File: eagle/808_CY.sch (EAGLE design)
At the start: 115 parts, among them IC1 TL071P, IC2 TL071P, IC3 TL071P, IC4 TL072P, Q1 2N3904, Q2 2N3904, Q3 2N3904, Q4 2N3904, Q5 2N3904, Q6 2N3904, Q7 2N3904, Q8 2N3906

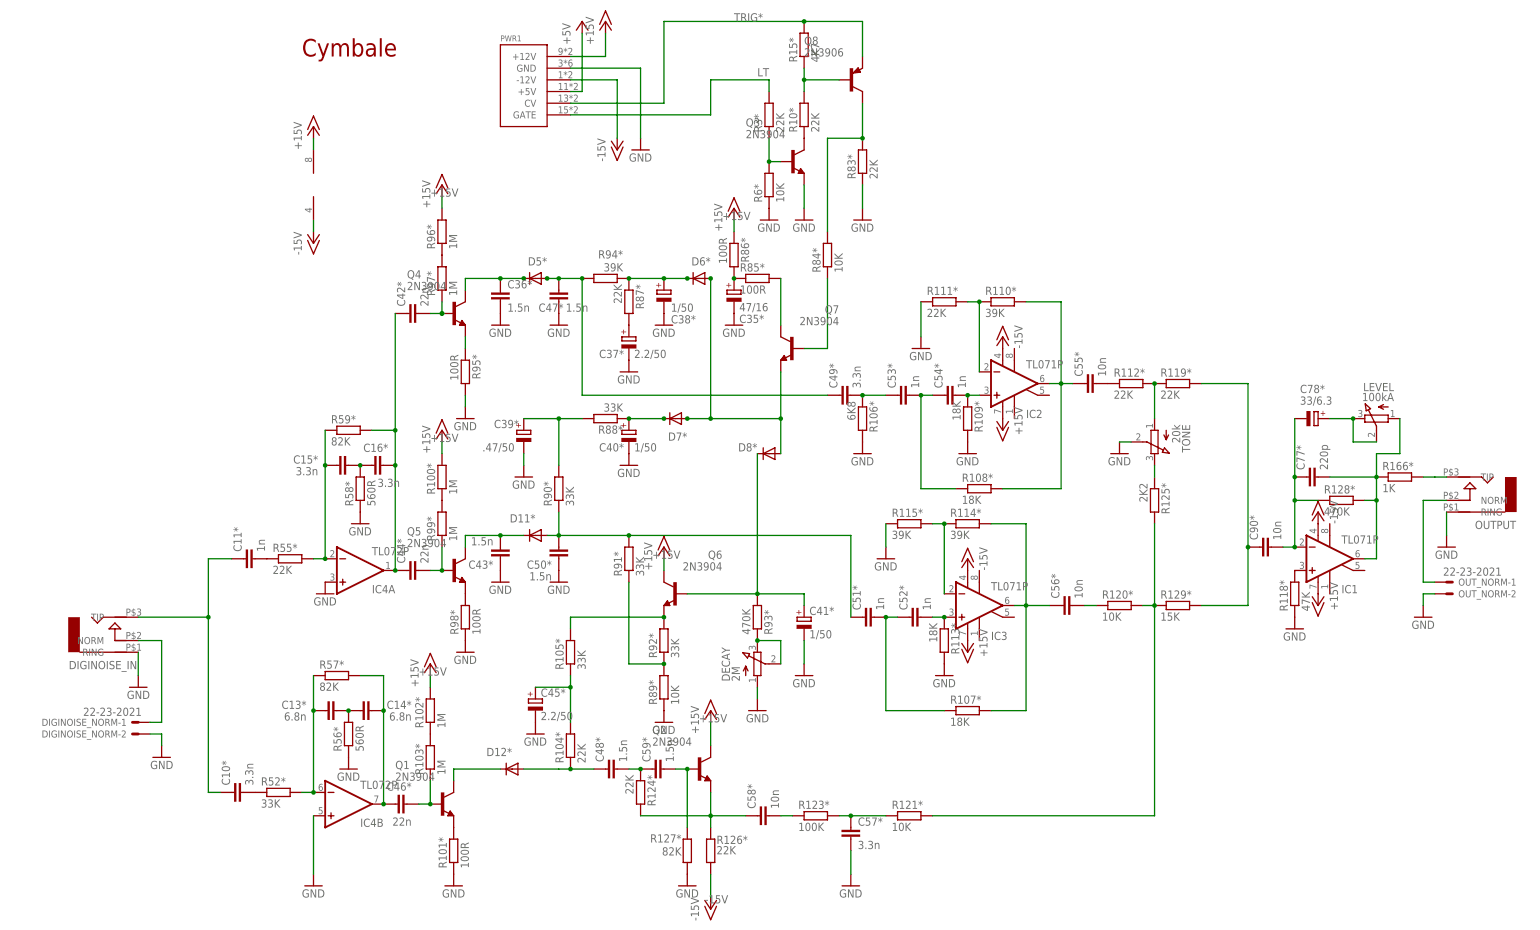
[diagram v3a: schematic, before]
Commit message: consolidated double 1m resistors
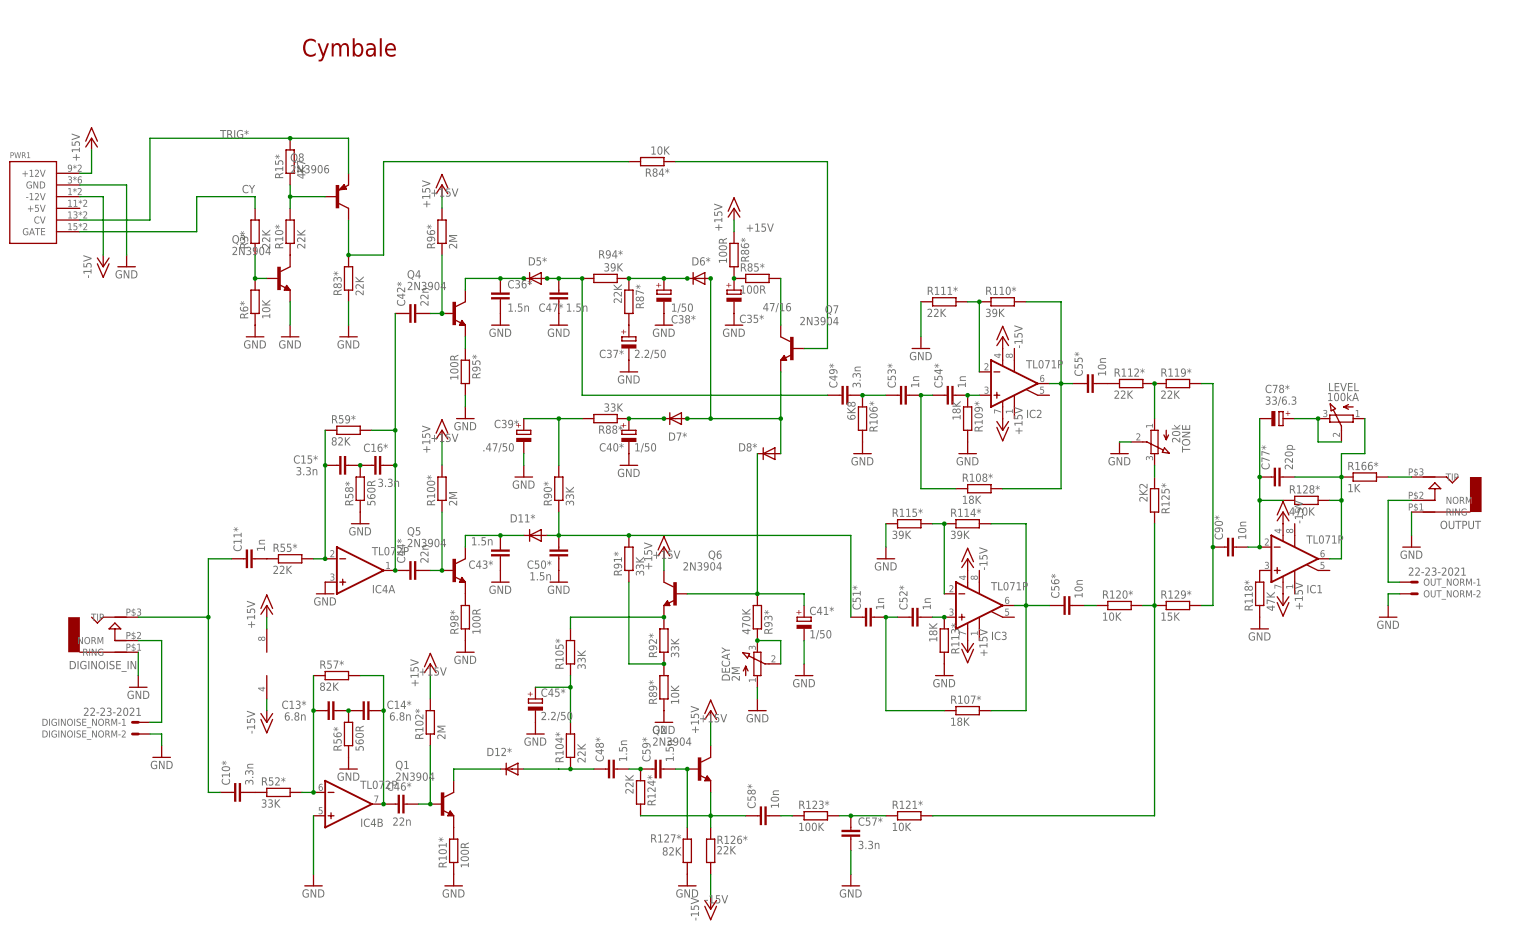
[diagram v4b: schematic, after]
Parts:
- removed R103*: 1M, TR808clone:R-EU_0207/2V
- removed R97*, R99*: 1M, TR808clone:R-EU_0207/5V
- R100*, R102*, R96*: value 1M -> 2M
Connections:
- net LT renamed CY
- removed net +5V: PWR1.+5V
- removed net CY_OUT: R166*.2
- removed net LT_LC_OUT: OUTPUT.TIP
- removed net N$176: R102*.1, R103*.2
- removed net N$180: R100*.1, R99*.2
- removed net N$181: R96*.1, R97*.2
- new net N$7: OUTPUT.TIP, R166*.2
- net N$498: now also R100*.1; no longer R99*.1
- net N$505: now also R102*.1; no longer R103*.1
- net N$524: now also R96*.1; no longer R97*.1
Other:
- moved on the sheet: C77*, C78*, C90*, IC1, LEVEL, OUTPUT, OUT_NORM-1, OUT_NORM-2, PWR1, Q3, Q8, R10*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

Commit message: third of the parts on
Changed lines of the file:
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@@
 <sheet>
 <plain>
-<text x="-33.02" y="149.86" size="3.81" layer="94">Cymbale</text>
+<text x="137.16" y="121.92" size="3.81" layer="94">Cymbale</text>
 </plain>
 <instances>

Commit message: 90 pct routed
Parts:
- R100*, R101*, R110*: device TR808clone:R-EU_0207/2V -> TR808clone:R-EU_0207/7
- R115*: device TR808clone:R-EU_0207/5V -> TR808clone:R-EU_0207/7
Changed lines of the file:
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@@
 <grid distance="0.1" unitdist="inch" unit="inch" style="lines" multiple="1" display="no" altdistance="0.01" altunitdist="inch" altunit="inch"/>
 <layers>
-<layer number="1" name="Top" color="1" fill="1" visible="no" active="no"/>
-<layer number="16" name="Bottom" color="4" fill="1" visible="no" active="no"/>
-<layer number="17" name="Pads" color="2" fill="1" visible="no" active="no"/>
-<layer number="18" name="Vias" color="2" fill="1" visible="no" active="no"/>
-<layer number="19" name="Unrouted" color="6" fill="1" visible="no" active="no"/>
-<layer number="20" name="Dimension" color="15" fill="1" visible="no" active="no"/>
-<layer number="21" name="tPlace" color="7" fill="1" visible="no" active="no"/>
-<layer number="22" name="bPlace" color="7" fill="1" visible="no" active="no"/>
-<layer number="23" name="tOrigins" color="15" fill="1" visible="no" active="no"/>
-<layer number="24" name="bOrigins" color="15" fill="1" visible="no" active="no"/>
-<layer number="25" name="tNames" color="7" fill="1" visible="no" active="no"/>
-<layer number="26" name="bNames" color="7" fill="1" visible="no" active="no"/>
-<layer number="27" name="tValues" color="7" fill="1" visible="no" active="no"/>
-<layer number="28" name="bValues" color="7" fill="1" visible="no" active="no"/>
-<layer number="29" name="tStop" color="7" fill="6" visible="no" active="no"/>
-<layer number="30" name="bStop" color="7" fill="3" visible="no" active="no"/>
-<layer number="31" name="tCream" color="7" fill="5" visible="no" active="no"/>
-<layer number="32" name="bCream" color="7" fill="4" visible="no" active="no"/>
+<layer number="1" name="Top" color="4" fill="1" visible="yes" active="no"/>
+<layer number="16" name="Bottom" color="1" fill="1" visible="yes" active="no"/>
+<layer number="17" name="Pads" color="2" fill="1" visible="yes" active="no"/>
+<layer number="18" name="Vias" color="2" fill="1" visible="yes" active="no"/>
+<layer number="19" name="Unrouted" color="6" fill="1" visible="yes" active="no"/>
+<layer number="20" name="Dimension" color="15" fill="1" visible="yes" active="no"/>
+<layer number="21" name="tPlace" color="7" fill="1" visible="yes" active="no"/>
+<layer number="22" name="bPlace" color="7" fill="1" visible="yes" active="no"/>
+<layer number="23" name="tOrigins" color="15" fill="1" visible="yes" active="no"/>
+<layer number="24" name="bOrigins" color="15" fill="1" visible="yes" active="no"/>
+<layer number="25" name="tNames" color="7" fill="1" visible="yes" active="no"/>
+<layer number="26" name="bNames" color="7" fill="1" visible="yes" active="no"/>
+<layer number="27" name="tValues" color="7" fill="1" visible="yes" active="no"/>
+<layer number="28" name="bValues" color="7" fill="1" visible="yes" active="no"/>
+<layer number="29" name="tStop" color="7" fill="3" visible="no" active="no"/>
+<layer number="30" name="bStop" color="7" fill="6" visible="no" active="no"/>
+<layer number="31" name="tCream" color="7" fill="4" visible="no" active="no"/>
+<layer number="32" name="bCream" color="7" fill="5" visible="no" active="no"/>
 <layer number="33" name="tFinish" color="6" fill="3" visible="no" active="no"/>
 <layer number="34" name="bFinish" color="6" fill="6" visible="no" active="no"/>
 <layer number="35" name="tGlue" color="7" fill="4" visible="no" active="no"/>
 <layer number="36" name="bGlue" color="7" fill="5" visible="no" active="no"/>
-<layer number="37" name="tTest" color="7" fill="1" visible="no" active="no"/>
-<layer number="38" name="bTest" color="7" fill="1" visible="no" active="no"/>
+<layer number="37" name="tTest" color="7" fill="1" visible="yes" active="no"/>
+<layer number="38" name="bTest" color="7" fill="1" visible="yes" active="no"/>
 <layer number="39" name="tKeepout" color="4" fill="11" visible="no" active="no"/>
 <layer number="40" name="bKeepout" color="1" fill="11" visible="no" active="no"/>
@@
 <layer number="44" name="Drills" color="7" fill="1" visible="no" active="no"/>
 <layer number="45" name="Holes" color="7" fill="1" visible="no" active="no"/>
-<layer number="46" name="Milling" color="3" fill="1" visible="no" active="no"/>
-<layer number="47" name="Measures" color="7" fill="1" visible="no" active="no"/>
-<layer number="48" name="Document" color="7" fill="1" visible="no" active="no"/>
-<layer number="49" name="Reference" color="7" fill="1" visible="no" active="no"/>
-<layer number="50" name="dxf" color="7" fill="1" visible="no" active="no"/>
-<layer number="51" name="tDocu" color="7" fill="1" visible="no" active="no"/>
-<layer number="52" name="bDocu" color="7" fill="1" visible="no" active="no"/>
-<layer number="53" name="tGND_GNDA" color="7" fill="9" visible="no" active="no"/>
-<layer number="54" name="bGND_GNDA" color="1" fill="9" visible="no" active="no"/>
-<layer number="56" name="wert" color="7" fill="1" visible="no" active="no"/>
-<layer number="57" name="tCAD" color="7" fill="1" visible="no" active="no"/>
-<layer number="59" name="tCarbon" color="7" fill="1" visible="no" active="no"/>
-<layer number="60" name="bCarbon" color="7" fill="1" visible="no" active="no"/>
+<layer number="46" name="Milling" color="3" fill="1" visible="yes" active="no"/>
+<layer number="47" name="Measures" color="7" fill="1" visible="yes" active="no"/>
+<layer number="48" name="Document" color="7" fill="1" visible="yes" active="no"/>
+<layer number="49" name="Reference" color="7" fill="1" visible="yes" active="no"/>
+<layer number="50" name="dxf" color="7" fill="1" visible="yes" active="no"/>
+<layer number="51" name="tDocu" color="7" fill="1" visible="yes" active="no"/>
+<layer number="52" name="bDocu" color="7" fill="1" visible="yes" active="no"/>
+<layer number="53" name="tGND_GNDA" color="7" fill="9" visible="yes" active="no"/>
+<layer number="54" name="bGND_GNDA" color="1" fill="9" visible="yes" active="no"/>
+<layer number="56" name="wert" color="7" fill="1" visible="yes" active="no"/>
+<layer number="57" name="tCAD" color="7" fill="1" visible="yes" active="no"/>
+<layer number="59" name="tCarbon" color="7" fill="1" visible="yes" active="no"/>
+<layer number="60" name="bCarbon" color="7" fill="1" visible="yes" active="no"/>
 <layer number="90" name="Modules" color="5" fill="1" visible="yes" active="yes"/>
 <layer number="91" name="Nets" color="2" fill="1" visible="yes" active="yes"/>
@@
 <part name="C46*" library="TR808clone" deviceset="C-EU" device="050-024X044" value="22n"/>
 <part name="V320" library="supply1" deviceset="GND" device=""/>
-<part name="R101*" library="TR808clone" deviceset="R-EU_" device="0207/2V" value="100R"/>
+<part name="R101*" library="TR808clone" deviceset="R-EU_" device="0207/7" value="100R"/>
 <part name="D12*" library="TR808clone" deviceset="1N4148" device="DO35-7"/>
 <part name="R104*" library="TR808clone" deviceset="R-EU_" device="0207/5V" value="22K"/>
@@
 <part name="R111*" library="TR808clone" deviceset="R-EU_" device="0207/5V" value="22K"/>
 <part name="V341" library="supply1" deviceset="GND" device=""/>
-<part name="R110*" library="TR808clone" deviceset="R-EU_" device="0207/2V" value="39K"/>
+<part name="R110*" library="TR808clone" deviceset="R-EU_" device="0207/7" value="39K"/>
 <part name="C55*" library="TR808clone" deviceset="C-EU" device="3.5MM_PITCH" value="10n"/>
 <part name="R112*" library="TR808clone" deviceset="R-EU_" device="0207/5V" value="22K"/>
 <part name="R119*" library="TR808clone" deviceset="R-EU_" device="0207/5V" value="22K"/>
 <part name="R125*" library="TR808clone" deviceset="R-EU_" device="0207/5V" value="2K2"/>
-<part name="R115*" library="TR808clone" deviceset="R-EU_" device="0207/5V" value="39K"/>
+<part name="R115*" library="TR808clone" deviceset="R-EU_" device="0207/7" value="39K"/>
 <part name="R114*" library="TR808clone" deviceset="R-EU_" device="0207/5V" value="39K"/>
 <part name="V343" library="supply1" deviceset="GND" device=""/>
@@
 <part name="V33" library="supply1" deviceset="GND" device=""/>
 <part name="R102*" library="TR808clone" deviceset="R-EU_" device="0207/2V" value="2M"/>
-<part name="R100*" library="TR808clone" deviceset="R-EU_" device="0207/2V" value="2M"/>
+<part name="R100*" library="TR808clone" deviceset="R-EU_" device="0207/7" value="2M"/>
 <part name="R96*" library="TR808clone" deviceset="R-EU_" device="0207/5V" value="2M"/>
 <part name="R108*" library="TR808clone" deviceset="R-EU_" device="0207/5V" value="18K"/>

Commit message: tweaks
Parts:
- R106*, R109*, R89*, R98*: device TR808clone:R-EU_0207/2V -> TR808clone:R-EU_0207/5V
- R113*, R86*: device TR808clone:R-EU_0207/2V -> TR808clone:R-EU_0207/7
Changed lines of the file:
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@@
 <part name="C44*" library="TR808clone" deviceset="C-EU" device="050-024X044" value="22n"/>
 <part name="V314" library="supply1" deviceset="GND" device=""/>
-<part name="R98*" library="TR808clone" deviceset="R-EU_" device="0207/2V" value="100R"/>
+<part name="R98*" library="TR808clone" deviceset="R-EU_" device="0207/5V" value="100R"/>
 <part name="C43*" library="TR808clone" deviceset="C-EU" device="3.5MM_PITCH" value="1.5n"/>
 <part name="D11*" library="TR808clone" deviceset="1N4148" device="DO35-7"/>
@@
 <part name="C35*" library="TR808clone" deviceset="CPOL-EU" device="E2.5-5" value="47/16"/>
 <part name="V324" library="supply1" deviceset="GND" device=""/>
-<part name="R86*" library="TR808clone" deviceset="R-EU_" device="0207/2V" value="100R"/>
+<part name="R86*" library="TR808clone" deviceset="R-EU_" device="0207/7" value="100R"/>
 <part name="R85*" library="TR808clone" deviceset="R-EU_" device="0207/5V" value="100R"/>
 <part name="R84*" library="TR808clone" deviceset="R-EU_" device="0207/5V" value="10K"/>
@@
 <part name="R91*" library="TR808clone" deviceset="R-EU_" device="0207/5V" value="33K"/>
 <part name="R92*" library="TR808clone" deviceset="R-EU_" device="0207/5V" value="33K"/>
-<part name="R89*" library="TR808clone" deviceset="R-EU_" device="0207/2V" value="10K"/>
+<part name="R89*" library="TR808clone" deviceset="R-EU_" device="0207/5V" value="10K"/>
 <part name="V335" library="supply1" deviceset="GND" device=""/>
 <part name="C41*" library="TR808clone" deviceset="CPOL-EU" device="E2.5-5" value="1/50"/>
@@
 <part name="C53*" library="TR808clone" deviceset="C-EU" device="3.5MM_PITCH" value="1n"/>
 <part name="C49*" library="TR808clone" deviceset="C-EU" device="3.5MM_PITCH" value="3.3n"/>
-<part name="R106*" library="TR808clone" deviceset="R-EU_" device="0207/2V" value="6K8"/>
+<part name="R106*" library="TR808clone" deviceset="R-EU_" device="0207/5V" value="6K8"/>
 <part name="V339" library="supply1" deviceset="GND" device=""/>
-<part name="R109*" library="TR808clone" deviceset="R-EU_" device="0207/2V" value="18K"/>
+<part name="R109*" library="TR808clone" deviceset="R-EU_" device="0207/5V" value="18K"/>
 <part name="V340" library="supply1" deviceset="GND" device=""/>
 <part name="R111*" library="TR808clone" deviceset="R-EU_" device="0207/5V" value="22K"/>
@@
 <part name="V343" library="supply1" deviceset="GND" device=""/>
 <part name="C52*" library="TR808clone" deviceset="C-EU" device="3.5MM_PITCH" value="1n"/>
-<part name="R113*" library="TR808clone" deviceset="R-EU_" device="0207/2V" value="18K"/>
+<part name="R113*" library="TR808clone" deviceset="R-EU_" device="0207/7" value="18K"/>
 <part name="V344" library="supply1" deviceset="GND" device=""/>
 <part name="C51*" library="TR808clone" deviceset="C-EU" device="3.5MM_PITCH" value="1n"/>

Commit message: tweaks
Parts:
- D5*: value 1N4148DO35-7 -> 1N4148DO35-10; device TR808clone:1N4148DO35-7 -> TR808clone:1N4148DO35-10
- R102*, R58*: device TR808clone:R-EU_0207/2V -> TR808clone:R-EU_0207/7
- R55*, R95*: device TR808clone:R-EU_0207/5V -> TR808clone:R-EU_0207/7
- R90*: device TR808clone:R-EU_0207/2V -> TR808clone:R-EU_0207/5V
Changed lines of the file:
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@@
 <parts>
 <part name="C11*" library="TR808clone" deviceset="C-EU" device="3.5MM_PITCH" value="1n"/>
-<part name="R55*" library="TR808clone" deviceset="R-EU_" device="0207/5V" value="22K"/>
+<part name="R55*" library="TR808clone" deviceset="R-EU_" device="0207/7" value="22K"/>
 <part name="V311" library="supply1" deviceset="GND" device=""/>
 <part name="C15*" library="TR808clone" deviceset="C-EU" device="3.5MM_PITCH" value="3.3n"/>
@@
 <part name="C43*" library="TR808clone" deviceset="C-EU" device="3.5MM_PITCH" value="1.5n"/>
 <part name="D11*" library="TR808clone" deviceset="1N4148" device="DO35-7"/>
-<part name="R90*" library="TR808clone" deviceset="R-EU_" device="0207/2V" value="33K"/>
+<part name="R90*" library="TR808clone" deviceset="R-EU_" device="0207/5V" value="33K"/>
 <part name="C39*" library="TR808clone" deviceset="CPOL-EU" device="E2.5-5" value=".47/50"/>
 <part name="V315" library="supply1" deviceset="GND" device=""/>
@@
 <part name="C42*" library="TR808clone" deviceset="C-EU" device="050-024X044" value="22n"/>
 <part name="C36*" library="TR808clone" deviceset="C-EU" device="3.5MM_PITCH" value="1.5n"/>
-<part name="D5*" library="TR808clone" deviceset="1N4148" device="DO35-7"/>
+<part name="D5*" library="TR808clone" deviceset="1N4148" device="DO35-10" value="1N4148DO35-10"/>
 <part name="C47*" library="TR808clone" deviceset="C-EU" device="3.5MM_PITCH" value="1.5n"/>
 <part name="V329" library="supply1" deviceset="GND" device=""/>
 <part name="V330" library="supply1" deviceset="GND" device=""/>
-<part name="R95*" library="TR808clone" deviceset="R-EU_" device="0207/5V" value="100R"/>
+<part name="R95*" library="TR808clone" deviceset="R-EU_" device="0207/7" value="100R"/>
 <part name="V331" library="supply1" deviceset="GND" device=""/>
 <part name="R94*" library="TR808clone" deviceset="R-EU_" device="0207/5V" value="39K"/>
@@
 <part name="R121*" library="TR808clone" deviceset="R-EU_" device="0207/5V" value="10K"/>
 <part name="V349" library="supply1" deviceset="GND" device=""/>
-<part name="R58*" library="TR808clone" deviceset="R-EU_" device="0207/2V" value="560R"/>
+<part name="R58*" library="TR808clone" deviceset="R-EU_" device="0207/7" value="560R"/>
 <part name="R56*" library="TR808clone" deviceset="R-EU_" device="0207/5V" value="560R"/>
 <part name="R105*" library="TR808clone" deviceset="R-EU_" device="0207/5V" value="33K"/>
 <part name="V33" library="supply1" deviceset="GND" device=""/>
-<part name="R102*" library="TR808clone" deviceset="R-EU_" device="0207/2V" value="2M"/>
+<part name="R102*" library="TR808clone" deviceset="R-EU_" device="0207/7" value="2M"/>
 <part name="R100*" library="TR808clone" deviceset="R-EU_" device="0207/7" value="2M"/>
 <part name="R96*" library="TR808clone" deviceset="R-EU_" device="0207/5V" value="2M"/>
